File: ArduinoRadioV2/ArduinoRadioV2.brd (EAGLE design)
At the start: 67.3 x 49.5 mm, 10 parts, among them J1 SJ1-3525N, U1 TLV70033DDCT

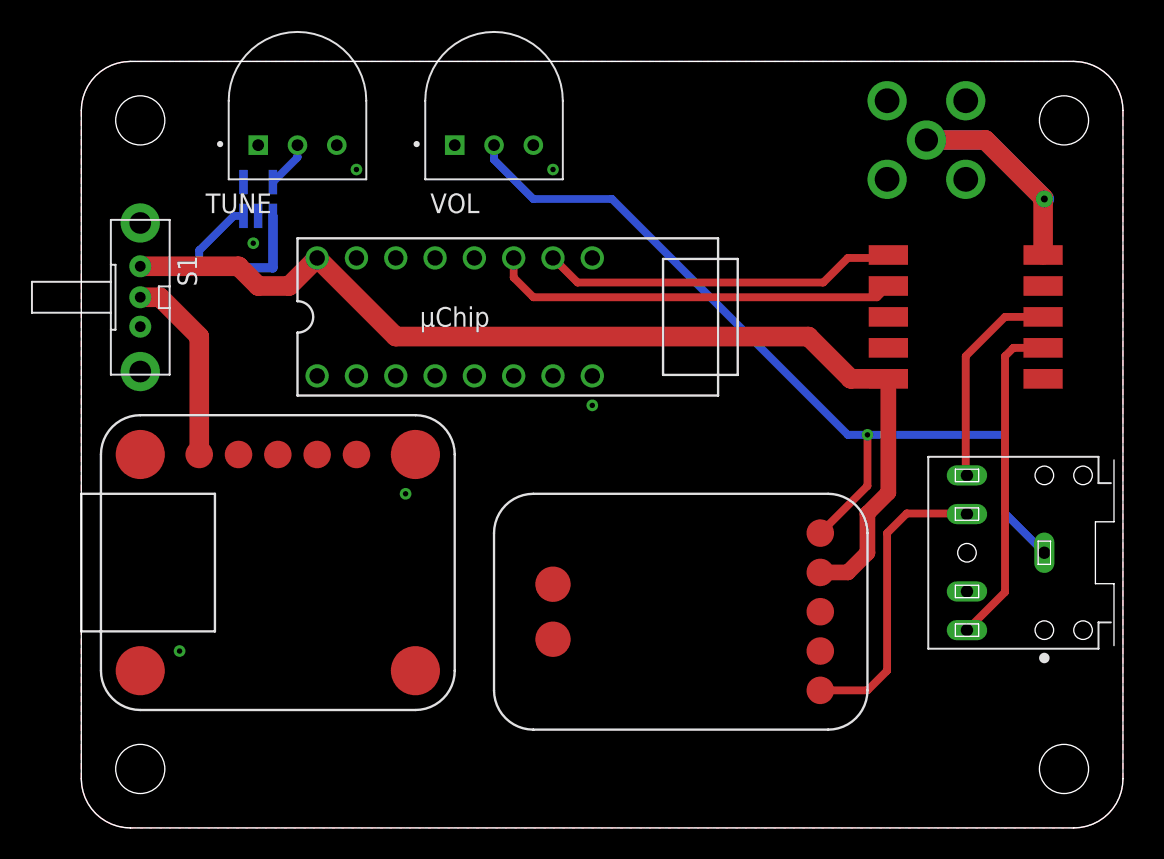
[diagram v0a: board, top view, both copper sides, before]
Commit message: Create BOM for V2 and label parts
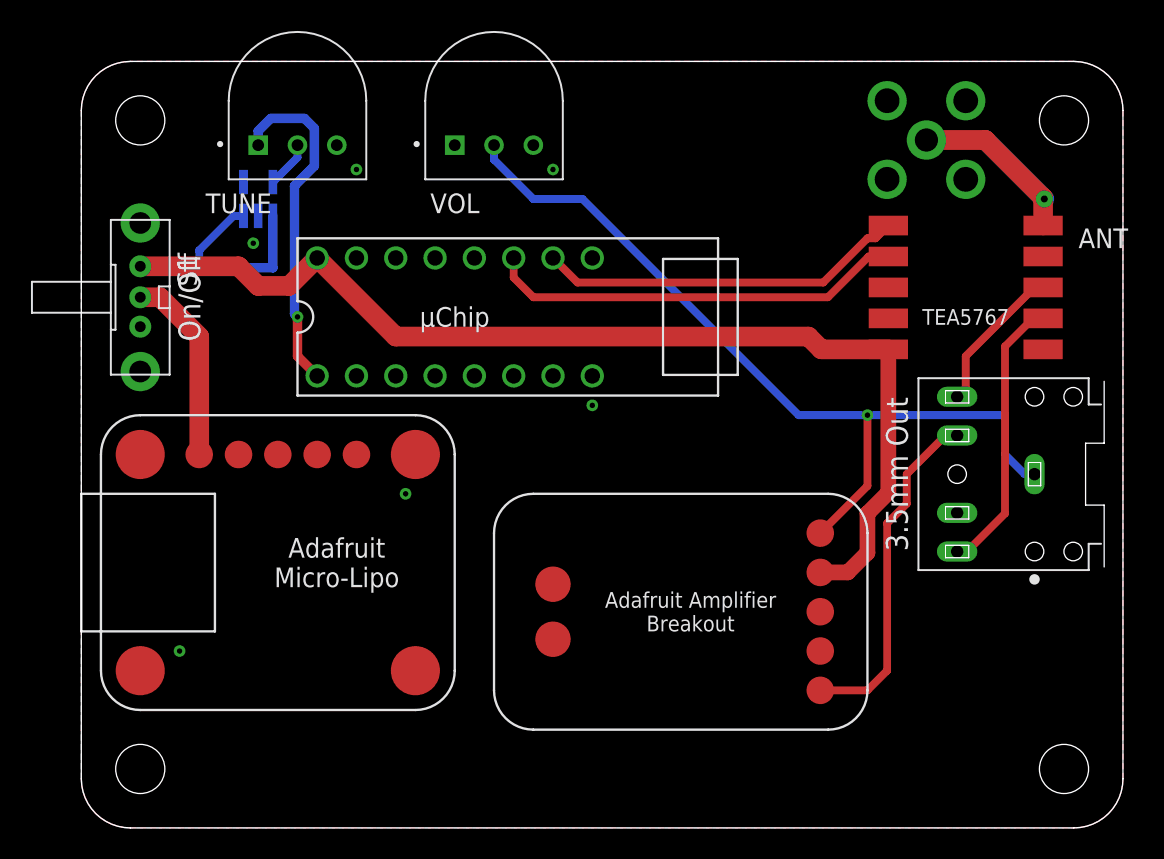
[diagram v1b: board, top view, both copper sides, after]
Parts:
- moved J1 5.12 mm to (61.6, 22.9)
- moved TEA5767 1.90 mm to (57.1, 34.9)
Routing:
- net N$2: track 0.00 -> 22.3 mm, vias 0 -> 1
- net LO: track 13.8 -> 9.69 mm
- net RO: track 21.4 -> 18.1 mm
- net VOL: track 57.6 -> 54.7 mm
- net AIN: track 19.4 -> 22.4 mm
- net ANT: track 22.0 -> 20.1 mm
- net 5V: track 85.1 -> 86.2 mm
- net SDA: track 23.1 -> 23.9 mm
- net SCL: track 26.3 -> 27.1 mm
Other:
- board text added: "3.3V REG"
- board text added: "3.5mm Out"
- board text added: "ANT"
- board text added: "Adafruit Amplifier Breakout"
- board text added: "Adafruit Micro-Lipo"
- board text added: "On/Off"
- board text added: "TEA5767"
